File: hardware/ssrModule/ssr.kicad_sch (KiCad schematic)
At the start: 113 parts, among them J1 Button-Sensors-MicroMatch2X03, J12 RJ45-CAN, J13 WAGO2604-1102, J2 WAGO2604-1108, J3 WAGO2604-1108, J5 IRDA, J6 IRDA, J7 RJ45-CAN, Q1 BC847, Q2 BC847, U1 PESD2CAN, U10 AQH3213A, U11 AQH3213A, U12 AQH3213A, U13 AQH3213A, U14 AQH3213A, U15 AQH3213A, U16 AQH3213A, U17 AQH3213A, U18 AQH3213A, U19 AQH3213A, U2 MCP2562-E-SN, U20 AQH3213A, U21 AQH3213A, U22 AQH3213A, U23 AQH3213A, U3 ESP32-WROOM-32, U4 MCP1703A-3302_SOT89, U5 PCF8574A, U6 PCF8574A, U7 AQH3213A, U8 AQH3213A, U9 wuerthDebug6

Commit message: feat: Add second fuse for ssr
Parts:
- added F2: 1A sehr träge, Fuse:Fuseholder_Cylinder-5x20mm_Schurter_0031_8201_Horizontal_Open, symbol Device:Fuse
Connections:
- net at F1.2, J13.1, J13.2: now also F2.2
- net AC renamed AC1
- net AC1: no longer U12.8, U13.8, U18.8, U19.8, U20.8, U21.8, U22.8, U23.8
- new net AC2: F2.1, U12.8, U13.8, U18.8, U19.8, U20.8, U21.8, U22.8, U23.8

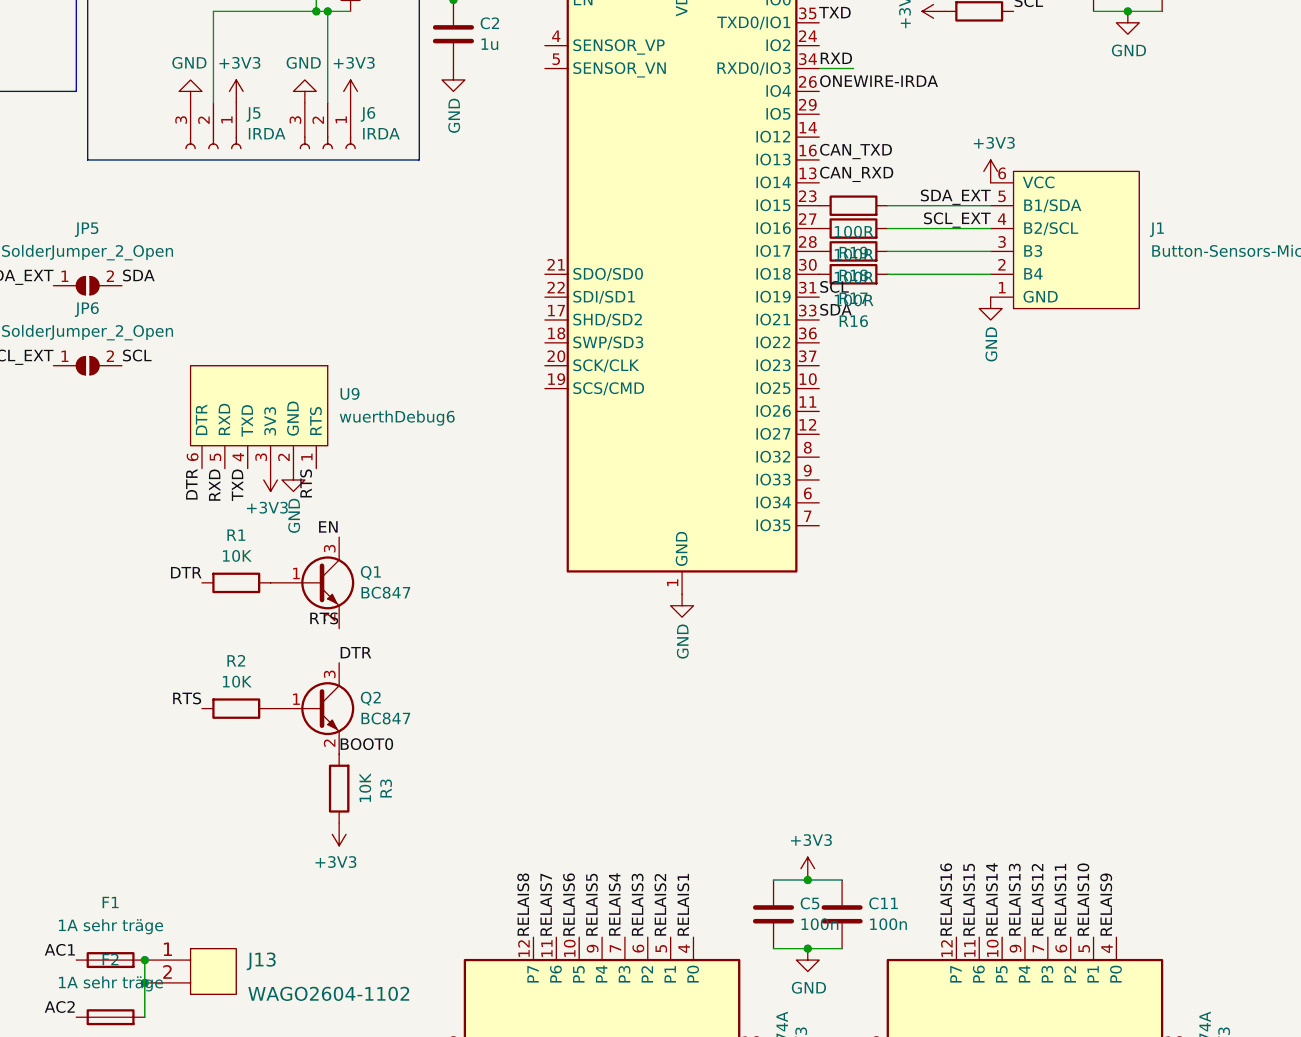
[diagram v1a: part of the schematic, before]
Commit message: feat: change PCB debug to EN/BOOT0
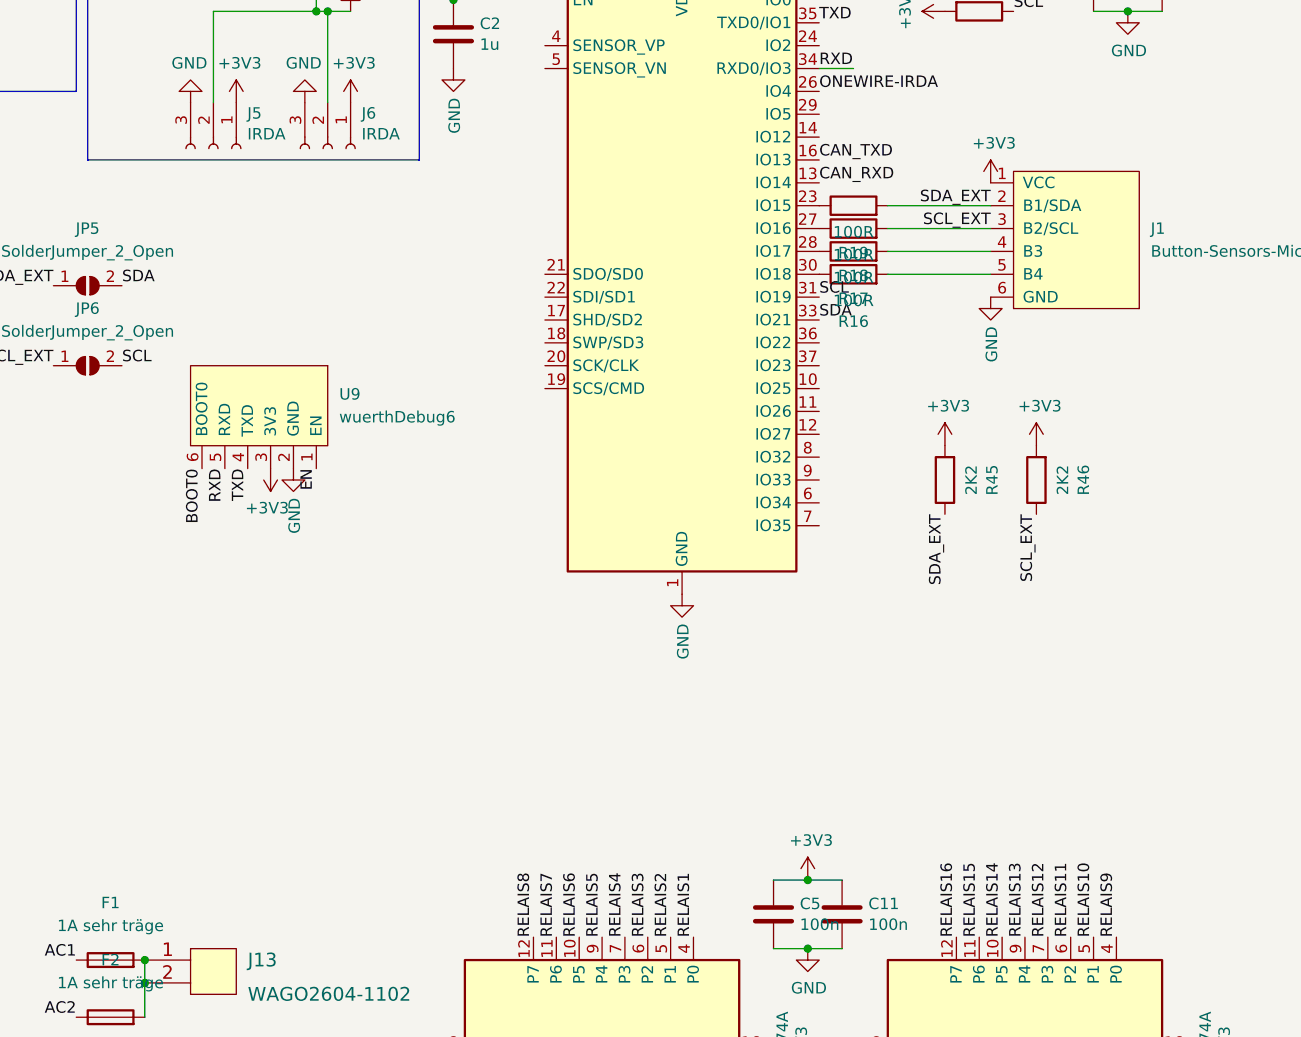
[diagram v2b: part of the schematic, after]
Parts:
- removed Q1, Q2: BC847, Package_TO_SOT_SMD:SOT-23, symbol Transistor_BJT:BC847
- removed R1, R2, R3: 10K, Resistor_SMD:R_0805_2012Metric_Pad1.20x1.40mm_HandSolder, symbol Device:R
- added R45, R46: 2K2, Resistor_SMD:R_0603_1608Metric_Pad0.98x0.95mm_HandSolder, symbol Device:R
- C1, C10, C11, C2, C4, C5, C8, C9: footprint Capacitor_SMD:C_0805_2012Metric_Pad1.18x1.45mm_HandSolder -> Capacitor_SMD:C_0603_1608Metric_Pad1.08x0.95mm_HandSolder
- D1, D10, D11, D12, D13, D14, D15, D16, D2, D3, D4, D5, D6, D7, D8, D9: footprint LED_SMD:LED_0805_2012Metric_Pad1.15x1.40mm_HandSolder -> LED_SMD:LED_0603_1608Metric_Pad1.05x0.95mm_HandSolder
- R10, R11, R12, R13, R14, R15, R16, R17, R18, R19, R20, R21, R22, R23, R24, R25, R26, R27, R28, R29, R30, R31, R32, R33, R34, R35, R36, R37, R38, R39, R4, R40, R41, R42, R43, R44, R5, R6, R7, R8, R9: footprint Resistor_SMD:R_0805_2012Metric_Pad1.20x1.40mm_HandSolder -> Resistor_SMD:R_0603_1608Metric_Pad0.98x0.95mm_HandSolder
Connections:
- net DTR is gone; now on net BOOT0: U9.6 (BOOT0)
- net RTS is gone; now on net EN: U9.1 (EN)
- net +3V3: now also J1.1 (VCC), R45.2, R46.2; no longer J1.6 (VCC)
- net GND: now also J1.6 (GND); no longer J1.1 (GND)
- net SCL_EXT: now also J1.3 (B2/SCL), R46.1; no longer J1.4 (B2/SCL)
- net SDA_EXT: now also J1.2 (B1/SDA), R45.1; no longer J1.5 (B1/SDA)
- net at R16.2: now also J1.5 (B4); no longer J1.2 (B4)
- net at R17.2: now also J1.4 (B3); no longer J1.3 (B3)
